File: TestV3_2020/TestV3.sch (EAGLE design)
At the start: 106 parts, among them Q1 600mA/40V, Q2 600mA/40V, Q3 600mA/40V, Q4 600mA/40V, U2 MP2451, U3 10k, U4 INA169

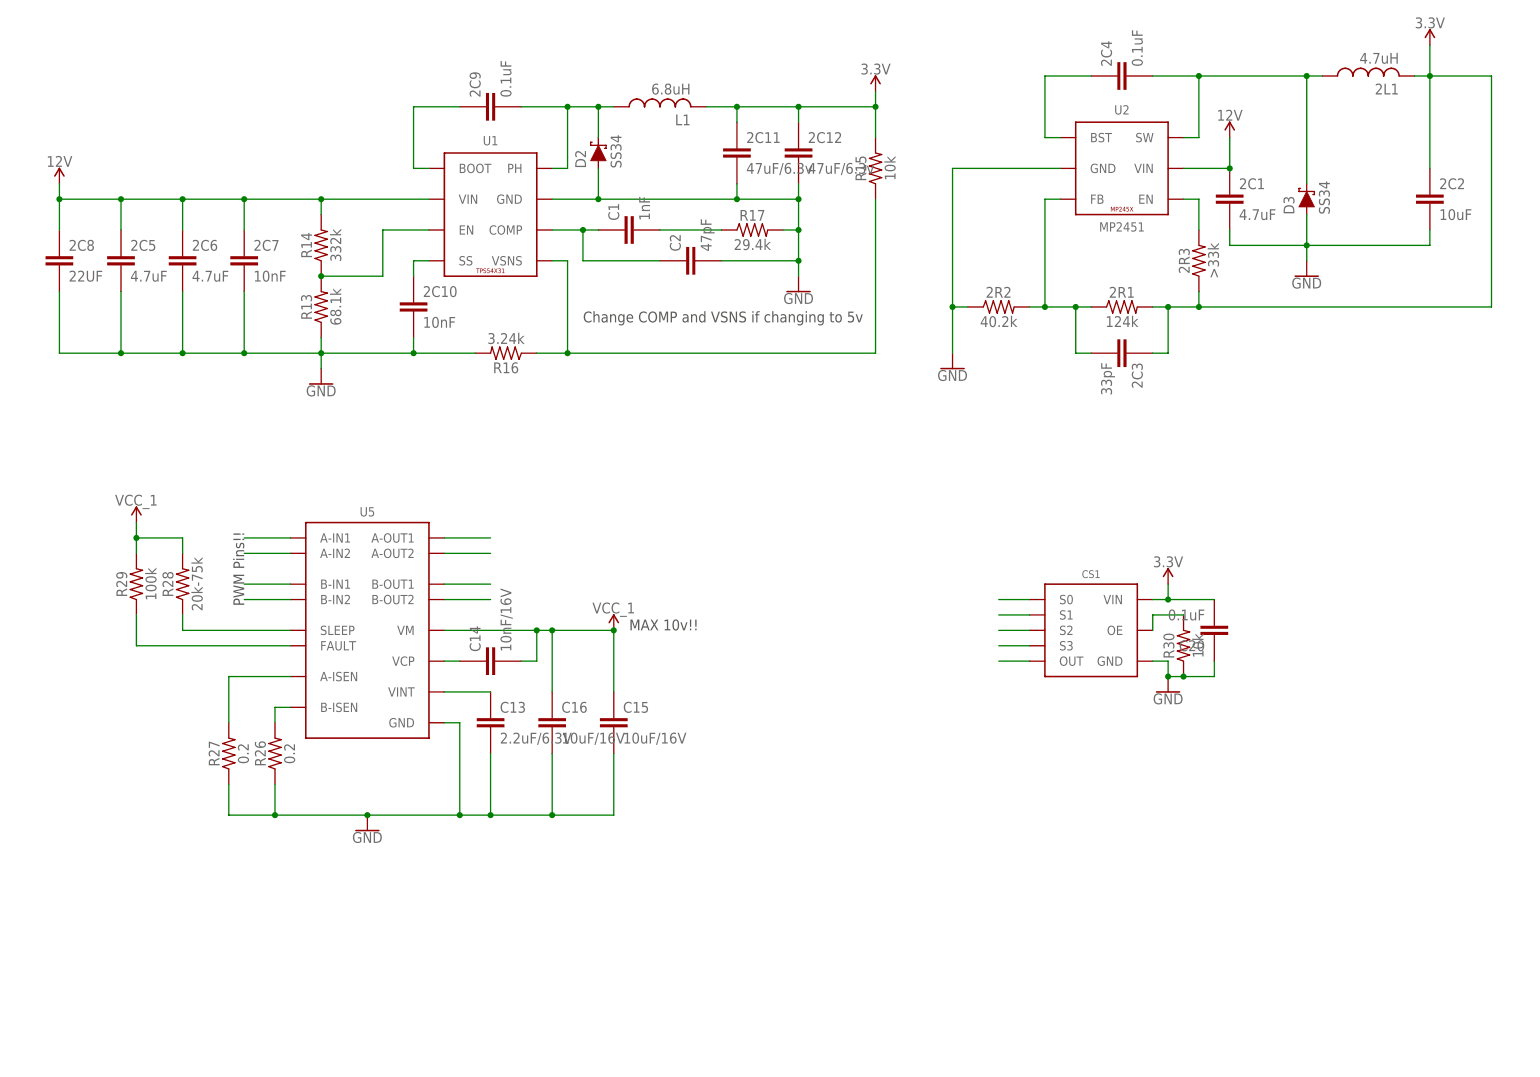
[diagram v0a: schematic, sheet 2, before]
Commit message: Finished TPS54331 Buck Converter Board Layout and Isolation Final Size ~2.2*2.2cm But I should probably add some test points and fix the silkscreen
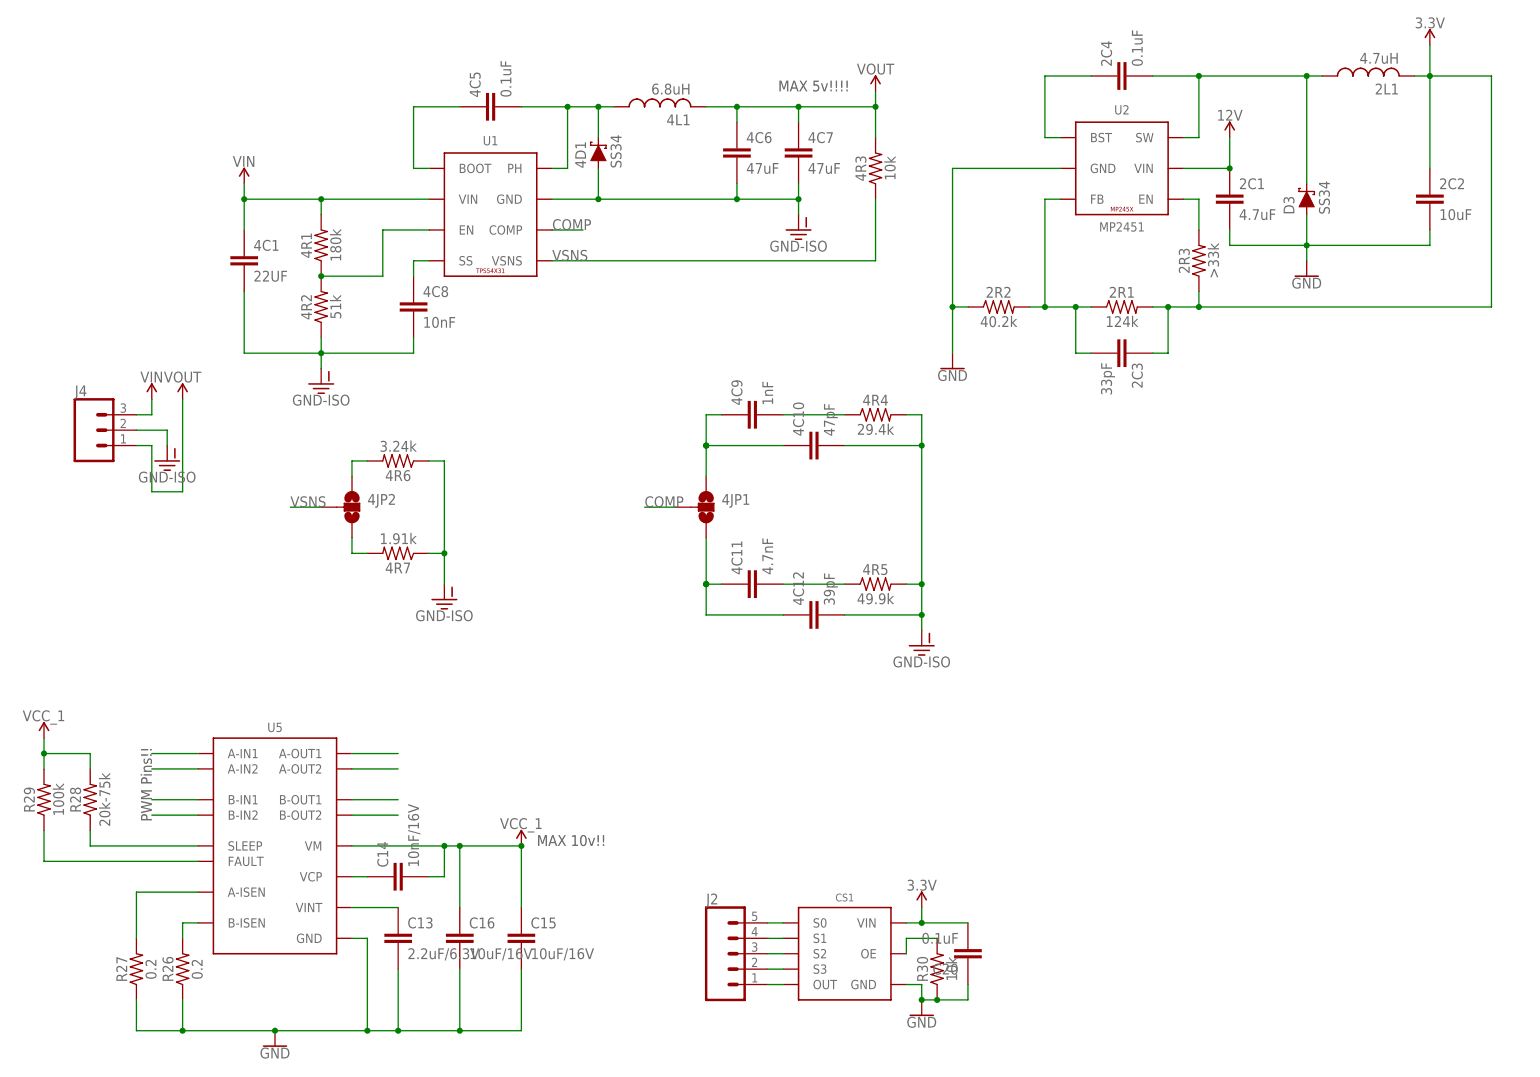
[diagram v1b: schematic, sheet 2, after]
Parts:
- removed 2C5, 2C6: 4.7uF, JH:CAPACITOR0603
- removed 2C7: 10nF, JH:CAPACITOR0603
- removed 2C8: 22UF, JH:CAPACITOR1210
- removed C1: 1nF, JH:CAPACITOR0603
- removed C2: 47pF, JH:CAPACITOR0603
- removed R16: 3.24k, JH:RESISTOR0603
- removed R17: 29.4k, JH:RESISTOR0603
- added 4C1: 22UF, JH:CAPACITOR1210
- added 4C10: 47pF, JH:CAPACITOR0603
- added 4C11: 4.7nF, JH:CAPACITOR0603
- added 4C12: 39pF, JH:CAPACITOR0603
- added 4C9: 1nF, JH:CAPACITOR0603
- added 4JP1, 4JP2: JUMPER-SMT_3_NO_SILK, SparkFun-Jumpers:JUMPER-SMT_3_NO_SILK
- added 4R4: 29.4k, JH:RESISTOR0603
- added 4R5: 49.9k, JH:RESISTOR0603
- added 4R6: 3.24k, JH:RESISTOR0603
- added 4R7: 1.91k, JH:RESISTOR0603
- added J2: (no value), SparkFun-Connectors:CONN_05LOCK
- added J4: (no value), SparkFun-Connectors:CONN_03LOCK
- 4C6, 4C7: value 47uF/6.3v -> 47uF
- 4R1: value 332k -> 180k
- 4R2: value 68.1k -> 51k
- renumbered 2C10 to 4C8, 2C11 to 4C6, 2C12 to 4C7, 2C9 to 4C5, D2 to 4D1, L1 to 4L1, R13 to 4R2, R14 to 4R1, R15 to 4R3
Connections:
- removed net N$13: 4R3.1, R16.1, U1.VSNS
- new net COMP: 4JP1.2, U1.COMP
- new net GND-ISO: 4C1.2, 4C10.2, 4C12.2, 4C6.2, 4C7.2, 4C8.2, 4D1.A, 4R2.1, 4R4.2, 4R5.2, 4R6.1, 4R7.1, J4.2, U1.GND
- new net N$52: 4C11.2, 4R5.1
- new net N$54: 4C11.1, 4C12.1, 4JP1.3
- new net N$57: 4JP2.1, 4R6.2
- new net N$58: 4JP2.3, 4R7.2
- new net VIN: 4C1.1, 4R1.2, J4.3, U1.VIN
- new net VOUT: 4C6.1, 4C7.1, 4L1.2, 4R3.2, J4.1
- new net VSNS: 4JP2.2, 4R3.1, U1.VSNS
- net 12V: no longer 2C5.1, 2C6.1, 2C7.1, 2C8.1, 4R1.2, U1.VIN
- net 3.3V: no longer 4C6.1, 4C7.1, 4L1.2, 4R3.2
- net GND: no longer 2C5.2, 2C6.2, 2C7.2, 2C8.2, 4C6.2, 4C7.2, 4C8.2, 4D1.A, 4R2.1, C2.2, R16.2, R17.2, U1.GND
- net N$12: now also 4C9.2, 4R4.1; no longer C1.2, R17.1
- net N$15: now also 4C10.1, 4C9.1, 4JP1.1; no longer C1.1, C2.1, U1.COMP
- net N$45: now also J2.5
- net N$46: now also J2.4
- net N$47: now also J2.3
- net N$48: now also J2.2
- net N$49: now also J2.1
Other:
- note added: "MAX 5v!!!!"
- note removed: "Change COMP and VSNS if changing to 5v"
- moved on the sheet: C13, C14, C15, C16, C20, CS1, R26, R27, R28, R29, R30, U5

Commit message: Added TCS3200 Datasheet and updated buck converter board layout fixed the silkscreen for buck converter and finalise design
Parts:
- removed 3C5: 0.1uF, JH:CAPACITOR0603
- removed C12, C17, C18, C4, C5, C6, C7: 1uF, JH:CAPACITOR0603
- removed C19: 4.7uF, JH:CAPACITOR0603
- removed D1: BLUE, SparkFun-LED:LED-BLUE0603
- removed D4: SS34, SparkFun-DiscreteSemi:DIODE-SCHOTTKY-B340A
- removed D5: SS34, SparkFun-DiscreteSemi:DIODE-SCHOTTKY-SS14
- removed FB1, FB2: 30Ω/1.8A, SparkFun-Coils:FERRITE_BEAD-0603
- removed J3: (no value), SparkFun-Connectors:USB_MICRO-B_FEMALE-SMT
- removed POT2: 10k, JH:3296-TRIMPOT
- removed R1, R2: 1k, JH:RESISTOR0603
- removed R19: 0.15, SparkFun-Resistors:RESISTOR0805
- removed R20: 3k, JH:RESISTOR0603
- removed R21, R9: 10k, JH:RESISTOR0603
- removed S1: 34-MOMENTARY-SWITCH, JH:34-MOMENTARY-SWITCH
- removed U$6: LM393, JH:LM393
- removed U4: INA169, SparkFun-IC-Special-Function:INA169
- removed U6: (no value), SparkFun-IC-Power:V_REG_LM1117SOT223
- removed UC1: STM32F103CBT6, JH:STM32F103CBT6
- added 1C1, 1C3, 1C6: 1uF, JH:CAPACITOR0603
- added 1C2, 1C4, 4C3: 10nF, JH:CAPACITOR0603
- added 1C5, 4C2: 4.7uF, JH:CAPACITOR0603
- added 1D1: BLUE, SparkFun-LED:LED-BLUE0603
- added 1FB1, 1FB2: 30Ω/1.8A, SparkFun-Coils:FERRITE_BEAD-0603
- added 1J1: USB-MICROB, JH:USB-MICROB
- added 1J2, 1J3: (no value), SparkFun-Connectors:CONN_20LOCK
- added 1R1, 1R2: 1k, JH:RESISTOR0603
- added 1R3: 10k, JH:RESISTOR0603
- added 1S1: 34-MOMENTARY-SWITCH, JH:34-MOMENTARY-SWITCH
- added 1U1: STM32F103CBT6, JH:STM32F103CBT6
- added 1U2: (no value), SparkFun-IC-Power:V_REG_LM1117SOT223
- added J10: (no value), SparkFun-Connectors:CONN_03-SCREW-5MM
- added J5: CONN_03, JH:CONN_03
- added J6: XT30UPB-F, JH:XT30UPB-F
- added J7: (no value), SparkFun-Connectors:CONN_07LOCK
- added J8: (no value), SparkFun-Connectors:CONN_025MM
- added J9: (no value), SparkFun-Connectors:CONN_02LOCK
- added R13: 20k, JH:RESISTOR0603
- 4C1: value 22UF -> 22uF
- 4C6, 4C7: device JH:CAPACITOR1210 -> JH:CAPACITOR1206
- 4D1, D3: device SparkFun-DiscreteSemi:DIODE-SCHOTTKY-SS14 -> JH:DIODE-SCHOTTKY
- 4JP1, 4JP2: value JUMPER-SMT_3_NO_SILK -> JUMPER-SMT_3_NO_NO-SILK; device SparkFun-Jumpers:JUMPER-SMT_3_NO_SILK -> SparkFun-Jumpers:JUMPER-SMT_3_NO_NO-SILK
- C13: value 2.2uF/6.3V -> 2.2uF
- C15, C16: value 10uF/16V -> 10uF; VOLTAGE (none) -> 16V
- J1: device SparkFun-Connectors:CONN_03LOCK -> SparkFun-Connectors:CONN_07LOCK
- J4: value (none) -> XT30UPB-F; device SparkFun-Connectors:CONN_03LOCK -> JH:XT30UPB-F
- U3: value 10k -> (none)
- renumbered C10 to 1C9, C11 to 1C10, C8 to 1C8, C9 to 1C7, OSC to 1OSC, Q1 to 1Q1, Q2 to 1Q2, R10 to 1R10, R11 to 1R11, R12 to 1R12, R3 to 1R4, R4 to 1R5, R5 to 1R6, R6 to 1R8, R7 to 1R7, R8 to 1R9, S2 to 1S2
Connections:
- removed net 12V: 2C1.1, 3C1.+, 3C5.1, 3L1.1, 3U1.VIN, C19.1, D4.C, R23.2, R24.2, R25.1, U2.VIN, U4.V+, U6.IN
- removed net 3.3V: 2C2.1, 2C3.1, 2L1.2, 2R1.2, 2R3.1, 3C3.1, C12.1, C20.2, CS1.VIN, POT2.CCW, R20.2, U$6G$1.P$V+, U3U1.VCC
- removed net N$14: 3C4.+, 3D1.C, C3.+, R18.2, R19.1, U4.VIN+
- removed net N$17: R21.2, U$6G$2.+IN, U4.OUT
- removed net N$19: D5.A, R20.1, U$6G$2.OUT
- removed net N$20: POT2.WIPER, U$6G$2.-IN
- removed net VCC_1: C14.2, C15.1, C16.1, R28.2, R29.2, U5.VM
- removed net VCC_2: R19.2, U4.VIN-
- new net GND-BOOST: 3C1.-, 3C2.2, 3C4.-, 3R2.1, 3U1.GND, C3.-, J10.2
- new net GND-BUCK: 2C1.2, 2C2.2, 2R2.1, D3.A, U2.GND
- new net GND-CS: C20.1, CS1.GND, J1.1, R30.1
- new net GND-LED: J9.1, Q3.E, Q4.E, R22.1
- new net GND-MOTOR: C13.2, C15.2, C16.2, J8.1, R26.1, R27.1, U5.GND
- new net GND-POT: 3C3.2, J2.1, U3U1.GND
- new net N$13: 1C5.1, 1U2.IN
- new net VCC-MOTOR: J7.1, R28.2, R29.2
- new net VIN-BOOST: 3C1.+, 3L1.1, 3U1.VIN, J10.3
- new net VIN-BUCK: 2C1.1, U2.VIN
- new net VIN-CS: C20.2, CS1.VIN, J1.2
- new net VIN-LED: J9.2, R23.2, R24.2, R25.1
- new net VIN-MOTOR: C14.2, C15.1, C16.1, J8.2, U5.VM
- new net VIN-POT: 3C3.1, J2.2, U3U1.VCC
- new net VOUT-BOOST: 3C4.+, 3D1.C, C3.+, J10.1, R18.2
- new net VOUT-BUCK: 2C2.1, 2C3.1, 2L1.2, 2R1.2, 2R3.1
- net 0: now also 1J2.2, 1U1.PB11/I2C2_SDA/USART3_RX; no longer UC1.PB11/I2C2_SDA/USART3_RX
- net 1: now also 1J2.3, 1U1.PB10/I2C2_SCL/USART3_TX; no longer UC1.PB10/I2C2_SCL/USART3_TX
- net 10: now also 1J2.12, 1U1.PA1/USART2_RTS/ADC12_IN1/TIM2_CH2; no longer UC1.PA1/USART2_RTS/ADC12_IN1/TIM2_CH2
- net 11: now also 1J2.13, 1U1.PA0_WKUP/USART2_CTS/ADC12_IN0/TIM2_CH1_ETR; no longer UC1.PA0_WKUP/USART2_CTS/ADC12_IN0/TIM2_CH1_ETR
- net 12: now also 1J2.15, 1U1.PC15-OSC32_OUT; no longer UC1.PC15-OSC32_OUT
- net 13: now also 1J2.16, 1U1.PC14-OSC32_IN; no longer UC1.PC14-OSC32_IN
- net 14: now also 1J2.17, 1U1.PC13-TAMPER-RTC; no longer UC1.PC13-TAMPER-RTC
- net 15: now also 1J3.4, 1U1.PB7/I2C1_SDA/TIM4_CH2; no longer UC1.PB7/I2C1_SDA/TIM4_CH2
- net 16: now also 1J3.5, 1U1.PB6/I2C1_SCL/TIM4_CH1; no longer UC1.PB6/I2C1_SCL/TIM4_CH1
- net 17: now also 1J3.6, 1U1.PB5/I2C1_SMBA; no longer UC1.PB5/I2C1_SMBA
- net 18: now also 1J3.7, 1U1.PB4/NJTRST; no longer UC1.PB4/NJTRST
- net 19: now also 1J3.8, 1U1.PB3/JTDO; no longer UC1.PB3/JTDO
- net 2: now also 1J2.4, 1U1.PB2/BOOT1; no longer UC1.PB2/BOOT1
- net 20: now also 1J3.9, 1U1.PA15/JTDI; no longer UC1.PA15/JTDI
- net 21: now also 1J3.10, 1U1.PA14/JTCK/SWCLK; no longer UC1.PA14/JTCK/SWCLK
- net 22: now also 1J3.11, 1U1.PA13/JTMS/SWDIO; no longer UC1.PA13/JTMS/SWDIO
- net 23_USBDP: now also 1J3.12, 1U1.PA12/USART1_RTS/CAN_TX/TIM1_ETR/USBDP; no longer UC1.PA12/USART1_RTS/CAN_TX/TIM1_ETR/USBDP
- net 24_USBDM: now also 1J3.13, 1U1.PA11/USART1_CTS/CAN_RX/TIM1_CH4/USBDM; no longer UC1.PA11/USART1_CTS/CAN_RX/TIM1_CH4/USBDM
- net 25: now also 1J3.14, 1U1.PA10/USART1_RX/TIM1_CH3; no longer UC1.PA10/USART1_RX/TIM1_CH3
- net 26: now also 1J3.15, 1U1.PA9/USART1_TX/TIM1_CH2; no longer UC1.PA9/USART1_TX/TIM1_CH2
- net 27: now also 1J3.16, 1U1.PA8/USART1_CK/TIM1_CH1/MCO; no longer UC1.PA8/USART1_CK/TIM1_CH1/MCO
- net 28: now also 1J3.17, 1U1.PB15/SPI2_MOSI/TIM1_CH3N; no longer UC1.PB15/SPI2_MOSI/TIM1_CH3N
- net 29: now also 1J3.18, 1U1.PB14/SPI2_MISO/USART3_RTS/TIM1_CH2N; no longer UC1.PB14/SPI2_MISO/USART3_RTS/TIM1_CH2N
- net 3: now also 1J2.5, 1U1.PB0/ADC12_IN8/TIM3_CH3; no longer UC1.PB0/ADC12_IN8/TIM3_CH3
- net 30: now also 1J3.19, 1U1.PB13/SPI2_SCK/USART3_CTS/TIM1_CH1N; no longer UC1.PB13/SPI2_SCK/USART3_CTS/TIM1_CH1N
- net 31: now also 1J3.20, 1U1.PB12/SPI2_NSS/I2C2_SMBA/USART3_CK/TIM1_BKIN; no longer UC1.PB12/SPI2_NSS/I2C2_SMBA/USART3_CK/TIM1_BKIN
- net 32: now also 1J3.3, 1R3.2, 1S1.2, 1U1.BOOT0, 1U1.PB8/TIM4_CH3; no longer R9.2, S1.2, UC1.BOOT0, UC1.PB8/TIM4_CH3
- net 33: now also 1R1.2, 1U1.PB1/ADC12_IN9/TIM3_CH4; no longer R1.2, UC1.PB1/ADC12_IN9/TIM3_CH4
- net 4: now also 1J2.6, 1U1.PA7/SPI1_MOSI/ADC12_IN7/TIM3_CH2; no longer UC1.PA7/SPI1_MOSI/ADC12_IN7/TIM3_CH2
- net 5: now also 1J2.7, 1U1.PA6/SPI1_MISO/ADC12_IN6/TIM3_CH1; no longer UC1.PA6/SPI1_MISO/ADC12_IN6/TIM3_CH1
- net 6: now also 1J2.8, 1U1.PA5/SPI1_SCK/ADC12_IN5; no longer UC1.PA5/SPI1_SCK/ADC12_IN5
- net 7: now also 1J2.9, 1U1.PA4/SPI1_NSS/USART2_CK/ADC12_IN4; no longer UC1.PA4/SPI1_NSS/USART2_CK/ADC12_IN4
- net 8: now also 1J2.10, 1U1.PA3/USART2_RX/ADC12_IN3/TIM2_CH4; no longer UC1.PA3/USART2_RX/ADC12_IN3/TIM2_CH4
- net 9: now also 1J2.11, 1U1.PA2/USART2_TX/ADC12_IN2/TIM2_CH3; no longer UC1.PA2/USART2_TX/ADC12_IN2/TIM2_CH3
- net AGND: now also 1C1.2, 1C2.2, 1FB2.2, 1J2.19, 1U1.VSS_A; no longer C18.2, C4.2, FB2.2, UC1.VSS_A
- net DISC: now also 1U1.PB9/TIM4_CH4; no longer UC1.PB9/TIM4_CH4
- net FDBK: now also R13.1; no longer D5.C
- net GND: now also 1C3.2, 1C4.2, 1C5.2, 1C6.2, 1D1.C, 1FB2.1, 1J1.GND, 1J3.2, 1R3.1, 1U1.VSS_1, 1U1.VSS_2, 1U1.VSS_3, 1U2.ADJ; no longer 2C1.2, 2C2.2, 2R2.1, 3C1.-, 3C2.2, 3C3.2, 3C4.-, 3C5.2, 3R2.1, 3U1.GND, C12.2, C13.2, C15.2, C16.2, C17.2, C19.2, C20.1, C3.-, C5.2, C6.2, C7.2, CS1.GND, D1.C, D3.A, FB2.1, J3.GND, POT2.CW, Q3.E, Q4.E, R21.1, R22.1, R26.1, R27.1, R30.1, R9.1, U$6G$1.P$V-, U2.GND, U3U1.GND, U4.GND, U5.GND, U6.ADJ, UC1.VSS_1, UC1.VSS_2, UC1.VSS_3
- net GND-ISO: now also 4C2.2, 4C3.2, J5.2; no longer J4.2
- net N$1: now also 1R2.1, 1S1.1; no longer R2.1, S1.1
- net N$18: now also R13.2
- net N$2: now also 1D1.A, 1R1.1; no longer D1.A, R1.1
- net N$22: now also J2.3; no longer J1.1
- net N$23: now also J2.4; no longer J1.2
- net N$24: now also J2.5; no longer J1.3
- net N$27: now also J7.7
- net N$29: now also J7.6
- net N$30: now also J7.5
- net N$31: now also J7.4
- net N$32: now also J7.3
- net N$33: now also J7.2
- net N$39: now also J4.P$V+
- net N$40: now also J4.P$V-
- net N$41: now also J6.P$V+
- net N$42: now also J6.P$V-
- net N$45: now also J1.7; no longer J2.5
- net N$46: now also J1.6; no longer J2.4
- net N$47: now also J1.5; no longer J2.3
- net N$48: now also J1.4; no longer J2.2
- net N$49: now also J1.3; no longer J2.1
- net N$59: now also 1J1.D-; no longer J3.D-
- net N$60: now also 1J1.D+; no longer J3.D+
- net OSC_IN: now also 1U1.PD0-OSC_IN; no longer UC1.PD0-OSC_IN
- net OSC_OUT: now also 1U1.PD1-OSC_OUT; no longer UC1.PD1-OSC_OUT
- net RESET: now also 1J2.14, 1U1.NRST; no longer UC1.NRST
- net VBAT: now also 1J2.18, 1U1.VBAT; no longer UC1.VBAT
- net VCC: now also 1C3.1, 1C4.1, 1C6.1, 1FB1.1, 1J3.1, 1R2.2, 1U1.VDD_1, 1U1.VDD_2, 1U1.VDD_3, 1U2.OUT, 1U2.OUT@1; no longer C17.1, C5.1, C6.1, C7.1, FB1.1, R2.2, U6.OUT, U6.OUT@1, UC1.VDD_1, UC1.VDD_2, UC1.VDD_3
- net VCCA: now also 1C1.1, 1C2.1, 1FB1.2, 1J2.20, 1U1.VDD_A; no longer C18.1, C4.1, FB1.2, UC1.VDD_A
- net VIN: now also 4C2.1, 4C3.1, J5.3; no longer J4.3
- net VOUT: now also J5.1; no longer J4.1
- net V_USB: now also 1J1.VBUS; no longer D4.A, J3.VBUS
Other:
- note added: "3.3v!"
- note removed: "Power supplies: 12/7.4V input 1 AVCC 250mA 1 DVCC 250mA (800mA for Rescue to power lights) 1 3.3v 3A Lights (For Soccer) 1 60v Solenoid (For Soccer)"

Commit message: finished stm32 board layout, the end is near!
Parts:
- added 1C11: 1uF, JH:CAPACITOR0603
- 1C4: value 10nF -> 1uF
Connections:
- net GND: now also 1C11.2
- net VCC: now also 1C11.1
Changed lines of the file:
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@@
 <drawing>
 <settings>
-<setting alwaysvectorfont="yes"/>
+<setting alwaysvectorfont="no"/>
 <setting verticaltext="up"/>
 </settings>
@@
 <part name="1C1" library="JH" library_urn="urn:adsk.eagle:library:6027132" deviceset="CAPACITOR" device="0603" package3d_urn="urn:adsk.eagle:package:15441226/3" value="1uF"/>
 <part name="1C2" library="JH" library_urn="urn:adsk.eagle:library:6027132" deviceset="CAPACITOR" device="0603" package3d_urn="urn:adsk.eagle:package:15441226/3" value="10nF"/>
-<part name="1C4" library="JH" library_urn="urn:adsk.eagle:library:6027132" deviceset="CAPACITOR" device="0603" package3d_urn="urn:adsk.eagle:package:15441226/3" value="10nF"/>
+<part name="1C4" library="JH" library_urn="urn:adsk.eagle:library:6027132" deviceset="CAPACITOR" device="0603" package3d_urn="urn:adsk.eagle:package:15441226/3" value="1uF"/>
 <part name="1C3" library="JH" library_urn="urn:adsk.eagle:library:6027132" deviceset="CAPACITOR" device="0603" package3d_urn="urn:adsk.eagle:package:15441226/3" value="1uF"/>
 <part name="1C7" library="JH" library_urn="urn:adsk.eagle:library:6027132" deviceset="CAPACITOR" device="0603" package3d_urn="urn:adsk.eagle:package:15441226/3" value="20pF"/>
@@
 <part name="P+2" library="SparkFun-PowerSymbols" library_urn="urn:adsk.eagle:library:530" deviceset="VCC" device=""/>
 <part name="U3" library="JH" library_urn="urn:adsk.eagle:library:6027132" deviceset="MCP41XXX" device="" package3d_urn="urn:adsk.eagle:package:6868027/1"/>
+<part name="1C11" library="JH" library_urn="urn:adsk.eagle:library:6027132" deviceset="CAPACITOR" device="0603" package3d_urn="urn:adsk.eagle:package:15441226/3" value="1uF"/>
 </parts>
 <sheets>
@@
 <instance part="P+2" gate="G$1" x="243.84" y="106.68" smashed="yes">
 <attribute name="VALUE" x="242.824" y="110.236" size="1.778" layer="96"/>
+</instance>
+<instance part="1C11" gate="G$1" x="182.88" y="132.08" smashed="yes" rot="MR0">
+<attribute name="NAME" x="181.356" y="135.001" size="1.778" layer="95" rot="MR0"/>
+<attribute name="VALUE" x="181.356" y="129.921" size="1.778" layer="96" rot="MR0"/>
 </instance>
 </instances>
@@
 <pinref part="1U1" gate="G$1" pin="VDD_3"/>
 <pinref part="1U1" gate="G$1" pin="VDD_2"/>
+<wire x1="172.72" y1="139.7" x2="182.88" y2="139.7" width="0.1524" layer="91"/>
+<junction x="172.72" y="139.7"/>
+<pinref part="1C11" gate="G$1" pin="1"/>
+<wire x1="182.88" y1="139.7" x2="182.88" y2="137.16" width="0.1524" layer="91"/>
 </segment>
 <segment>
@@
 <pinref part="1C3" gate="G$1" pin="2"/>
 <pinref part="SUPPLY14" gate="1" pin="GND"/>
-</segment>
-<segment>
+<pinref part="1C11" gate="G$1" pin="2"/>
+<wire x1="182.88" y1="127" x2="172.72" y2="127" width="0.1524" layer="91"/>
+</segment>
+<segment>

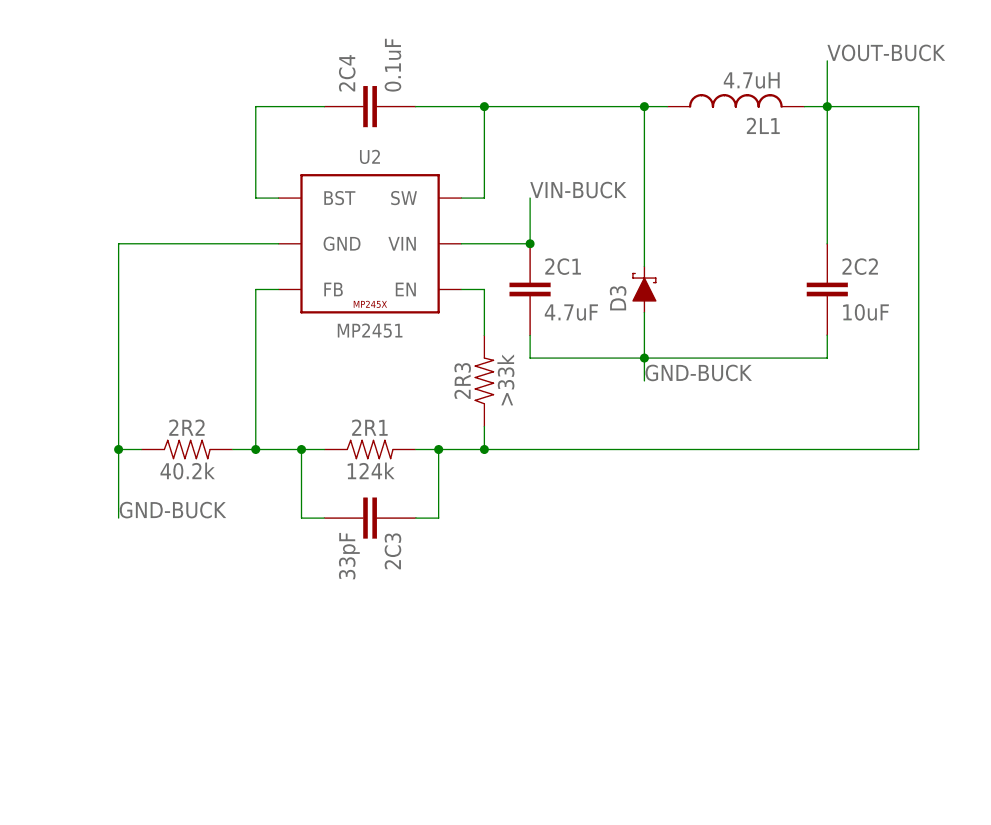
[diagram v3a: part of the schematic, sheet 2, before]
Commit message: MP2451 Buck Converter Circuit
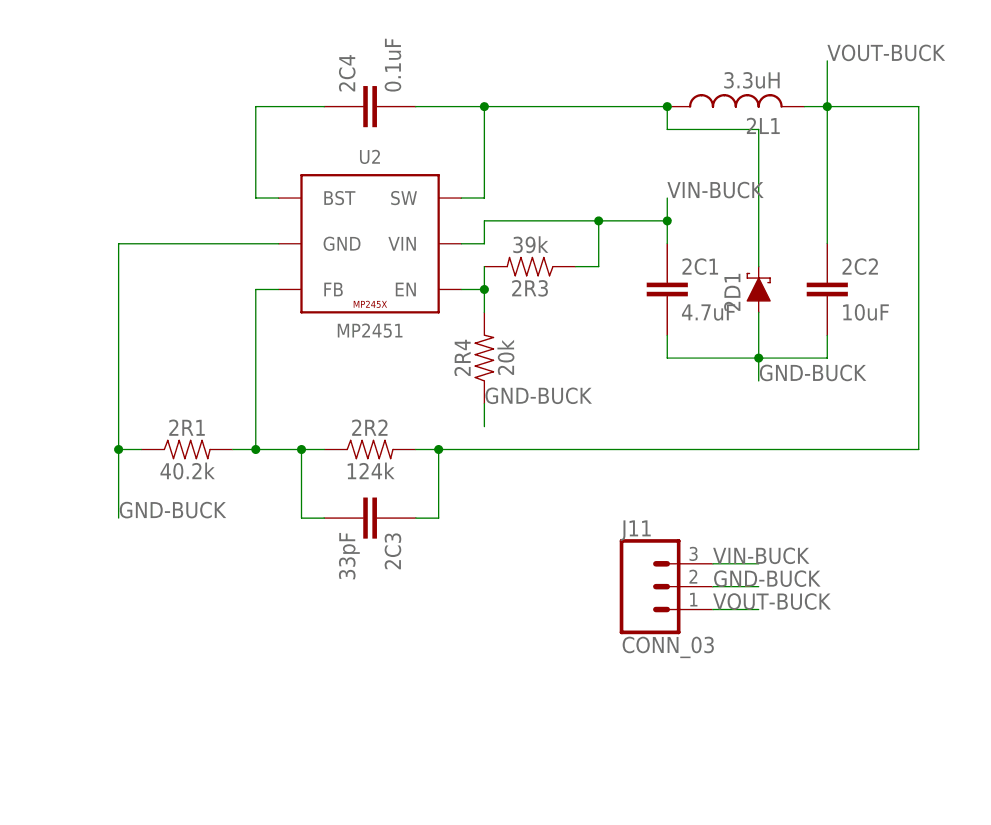
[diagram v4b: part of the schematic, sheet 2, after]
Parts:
- removed D3: SS34, JH:DIODE-SCHOTTKY
- added 2D1: SS34, JH:DIODE-SCHOTTKY
- added 2R4: 20k, JH:RESISTOR0603
- added J11: CONN_03, JH:CONN_03
- added J3: (no value), SparkFun-Connectors:CONN_02LOCK
- added U4: LIGHT_SENSORALS, SparkFun-Sensors:LIGHT_SENSORALS
- 2L1: value 4.7uH -> 3.3uH
- 2R1: value 124k -> 40.2k
- 2R2: value 40.2k -> 124k
- 2R3: value >33k -> 39k
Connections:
- removed net N$7: 2R3.2, U2.EN
- new net N$14: J3.2, U4.C1
- new net N$17: J3.1, U4.E1
- new net N$20: 2R3.2, 2R4.2, U2.EN
- net GND-BUCK: now also 2D1.A, 2R1.1, 2R4.1, J11.2; no longer 2R2.1, D3.A
- net N$3: now also 2R1.2, 2R2.1; no longer 2R1.1, 2R2.2
- net N$5: now also 2D1.C; no longer D3.C
- net VIN-BUCK: now also 2R3.1, J11.3
- net VOUT-BUCK: now also 2R2.2, J11.1; no longer 2R1.2, 2R3.1
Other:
- moved on the sheet: 2C1, 2R1, 2R2, 2R3
